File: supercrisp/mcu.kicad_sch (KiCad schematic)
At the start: 9 parts, among them P1 USB_C_Plug_USB2.0, U1 STM32F072CBTx, U2 USBLC6-2SC6

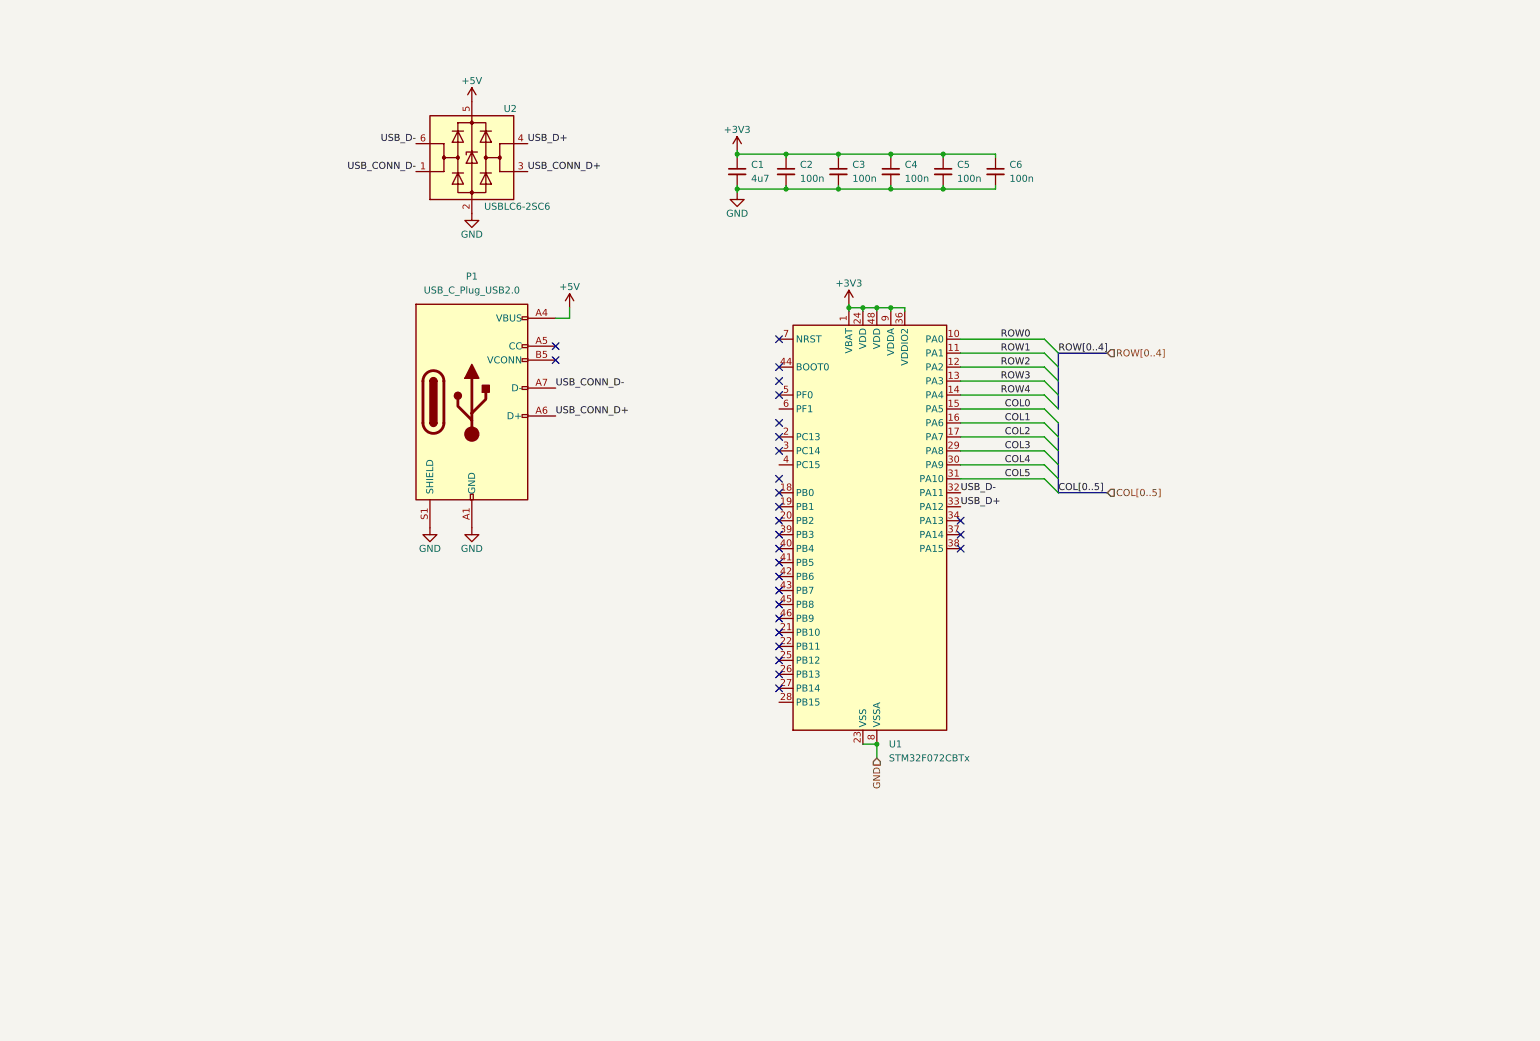
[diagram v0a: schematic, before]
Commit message: Add BOOT0 handling and start working on power schematics
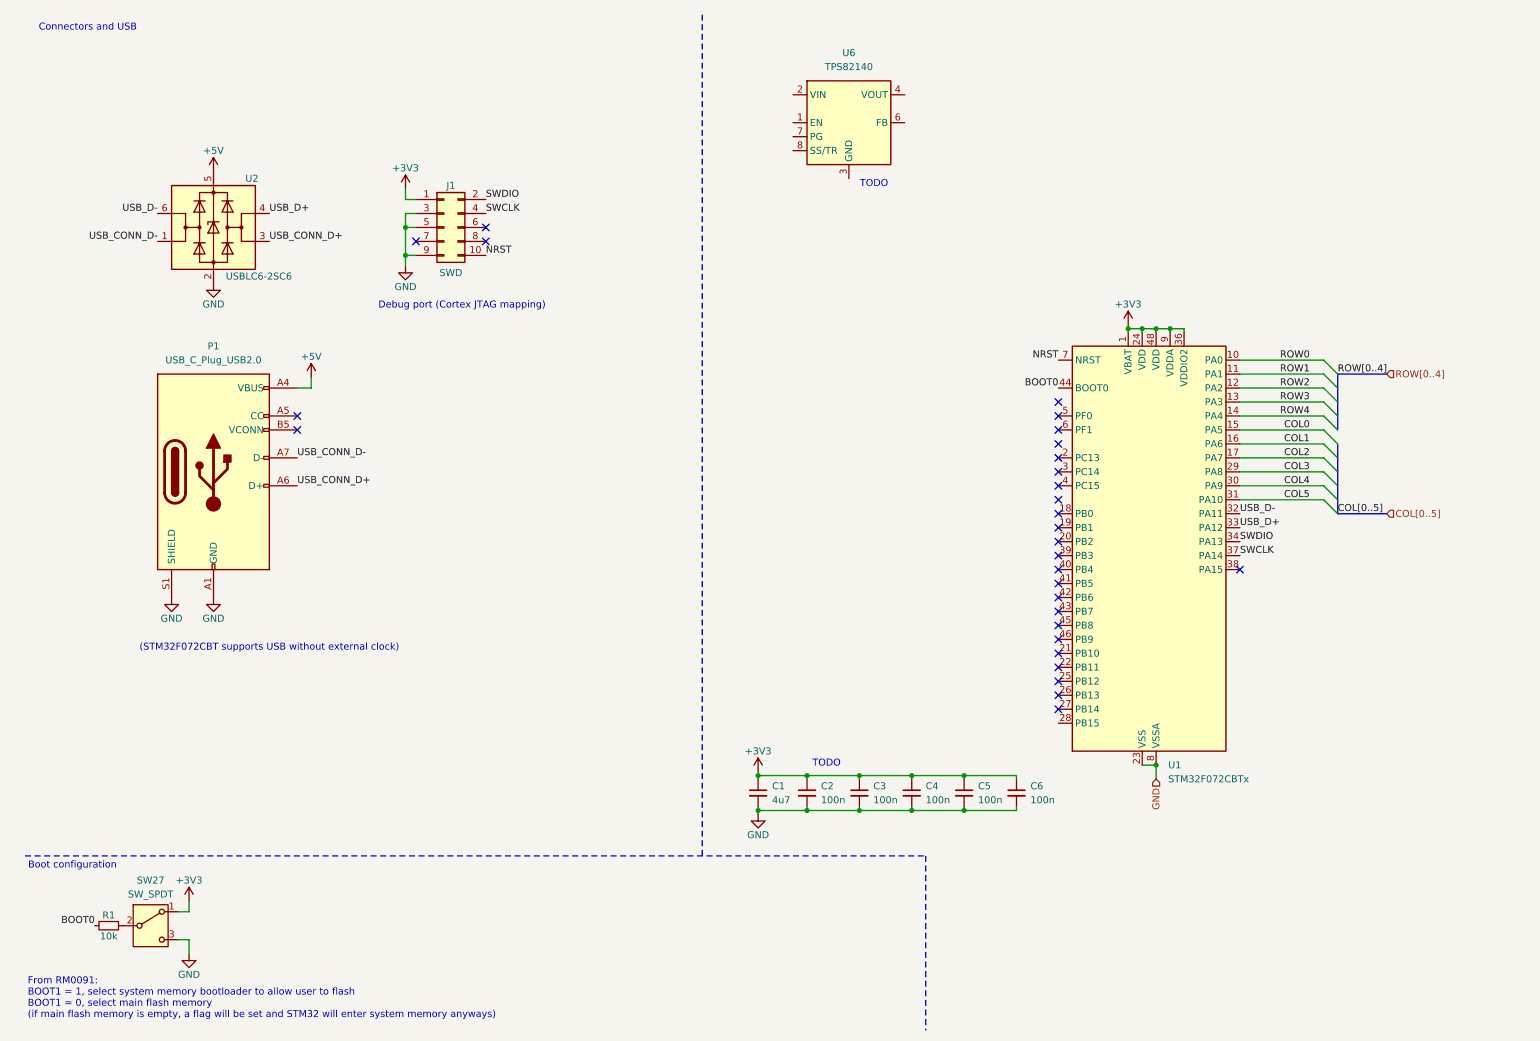
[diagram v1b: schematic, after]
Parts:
- added J1: SWD, Connector_PinHeader_1.27mm:PinHeader_2x05_P1.27mm_Vertical_SMD, symbol Connector_Generic:Conn_02x05_Odd_Even
- added R1: 10k, Resistor_SMD:R_0402_1005Metric, symbol Device:R_Small
- added SW27: SW_SPDT, Button_Switch_SMD:SW_SPDT_PCM12, symbol Switch:SW_SPDT
- added U6: TPS82140, Package_LGA:Texas_SIL0008D_MicroSiP-8-1EP_2.8x3mm_P0.65mm_EP1.1x1.9mm_ThermalVias, symbol Regulator_Switching:TPS82140
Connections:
- net +3V3: now also J1.1 (Pin_1), SW27.1 (A)
- net GND: now also J1.3 (Pin_3), J1.5 (Pin_5), J1.9 (Pin_9), SW27.3 (C)
- net SWDIO: now reaches U1.34 (PA13)
- net SWDIO: now also J1.2 (Pin_2)
- net SWCLK: now reaches U1.37 (PA14)
- net SWCLK: now also J1.4 (Pin_4)
- net BOOT0: now reaches U1.44 (BOOT0)
- net BOOT0: now also R1.2
- net NRST: now reaches U1.7 (NRST)
- net NRST: now also J1.10 (Pin_10)
- new net: U6.3 (GND), U6.9 (GND)
- new net: U6.4 (VOUT), U6.5 (VOUT)
- new net: R1.1, SW27.2 (B)
- no-connect marks 28 -> 29
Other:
- note added: "(STM32F072CBT supports USB without external clock)"
- note added: "Boot configuration"
- note added: "Connectors and USB"
- note added: "Debug port (Cortex JTAG mapping)"
- note added: "From RM0091: BOOT1 = 1, select system memory bootloader to allow user to flash BOOT1 = 0, select main flash memory (if main flash memory is empty, a flag will be set and STM32 will enter system memory anyways)"
- note added: "TODO"
- moved on the sheet: P1, U1, U2

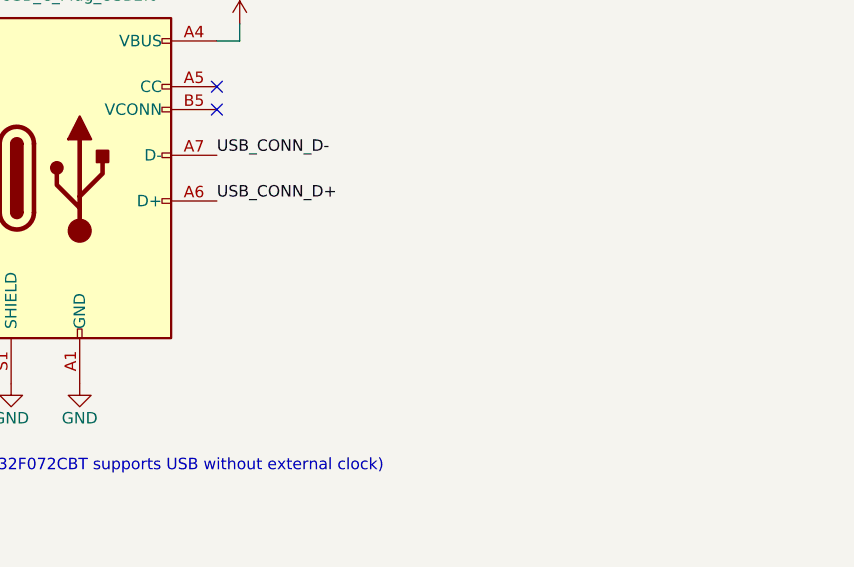
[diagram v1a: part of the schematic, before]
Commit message: Start adding USB C connector circuit
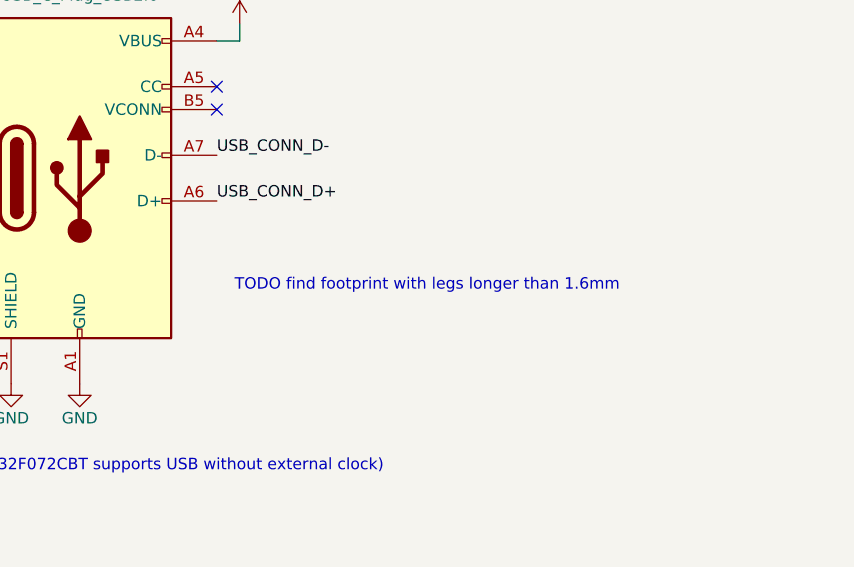
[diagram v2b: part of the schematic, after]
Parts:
- P1: footprint Connector_USB:USB_C_Receptacle_GCT_USB4125-xx-x-0190_6P_TopMnt_Horizontal -> Connector_USB:USB_C_Receptacle_XKB_U262-16XN-4BVC11
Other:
- note added: "TODO find footprint with legs longer than 1.6mm"
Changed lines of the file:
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@@
+		)
+	)
+	(text "TODO find footprint with legs longer than 1.6mm"
+		(exclude_from_sim no)
+		(at 85.598 108.458 0)
+		(effects
+			(font
+				(size 1.27 1.27)
+			)
 		)
 	)
@@
 			)
 		)
-		(property "Footprint" "Connector_USB:USB_C_Receptacle_GCT_USB4125-xx-x-0190_6P_TopMnt_Horizontal"
+		(property "Footprint" "Connector_USB:USB_C_Receptacle_XKB_U262-16XN-4BVC11"
 			(at 50.8 96.52 0)
 			(effects

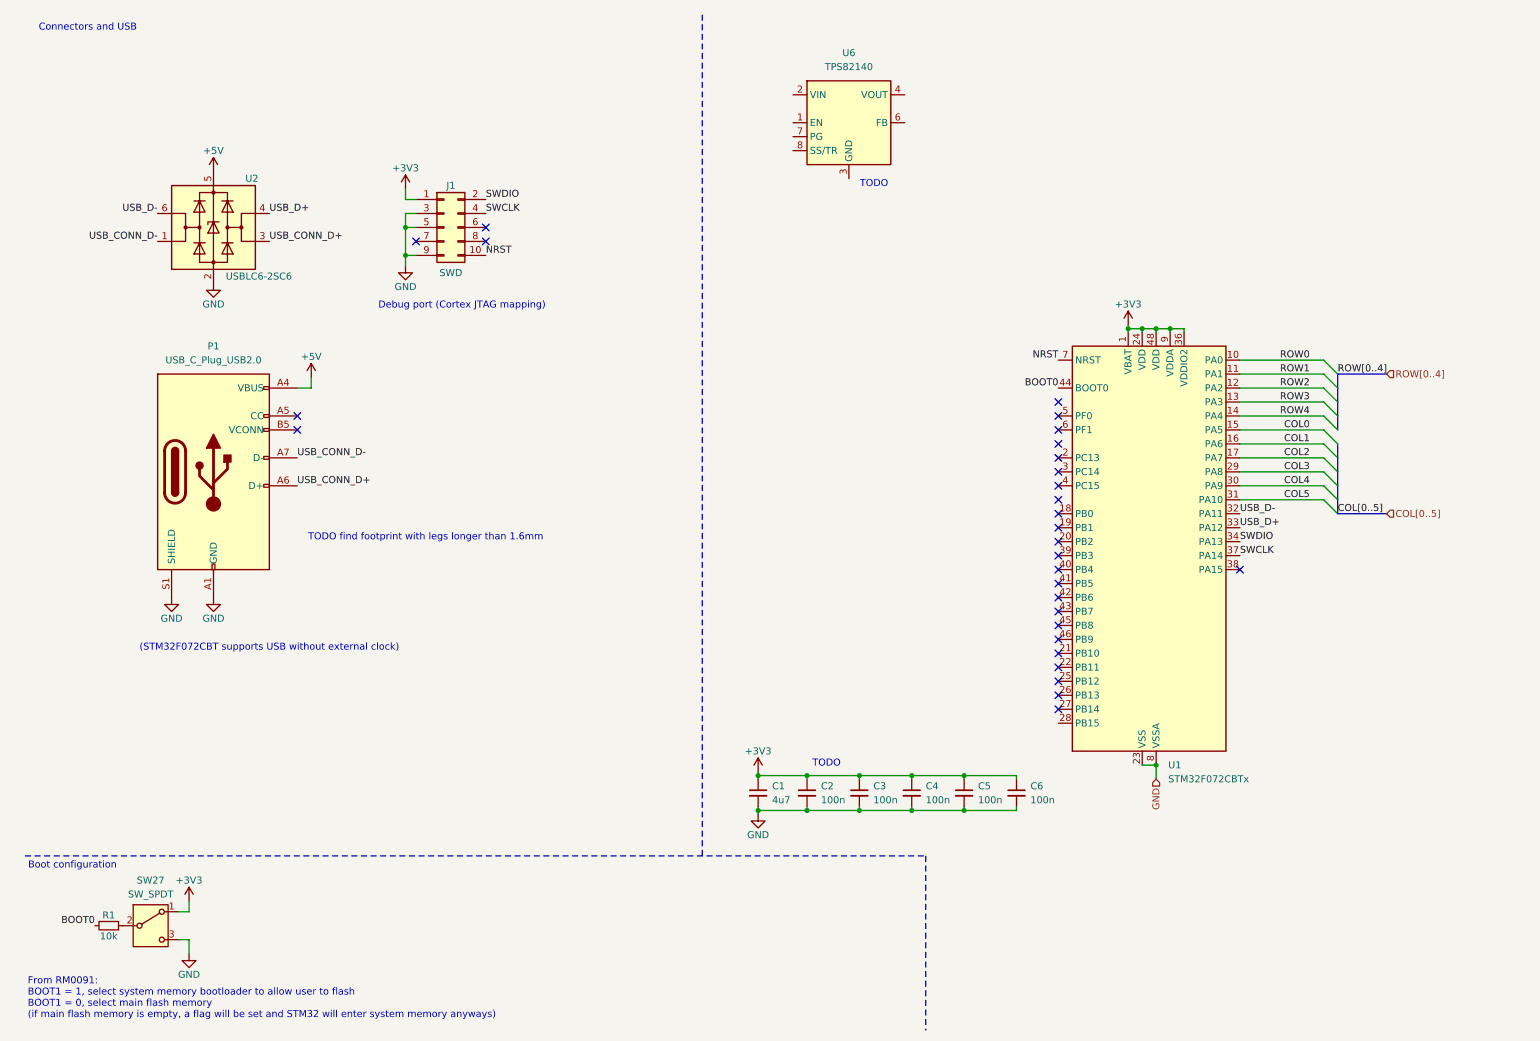
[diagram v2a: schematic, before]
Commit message: Temp placement of switches and usb circuitry
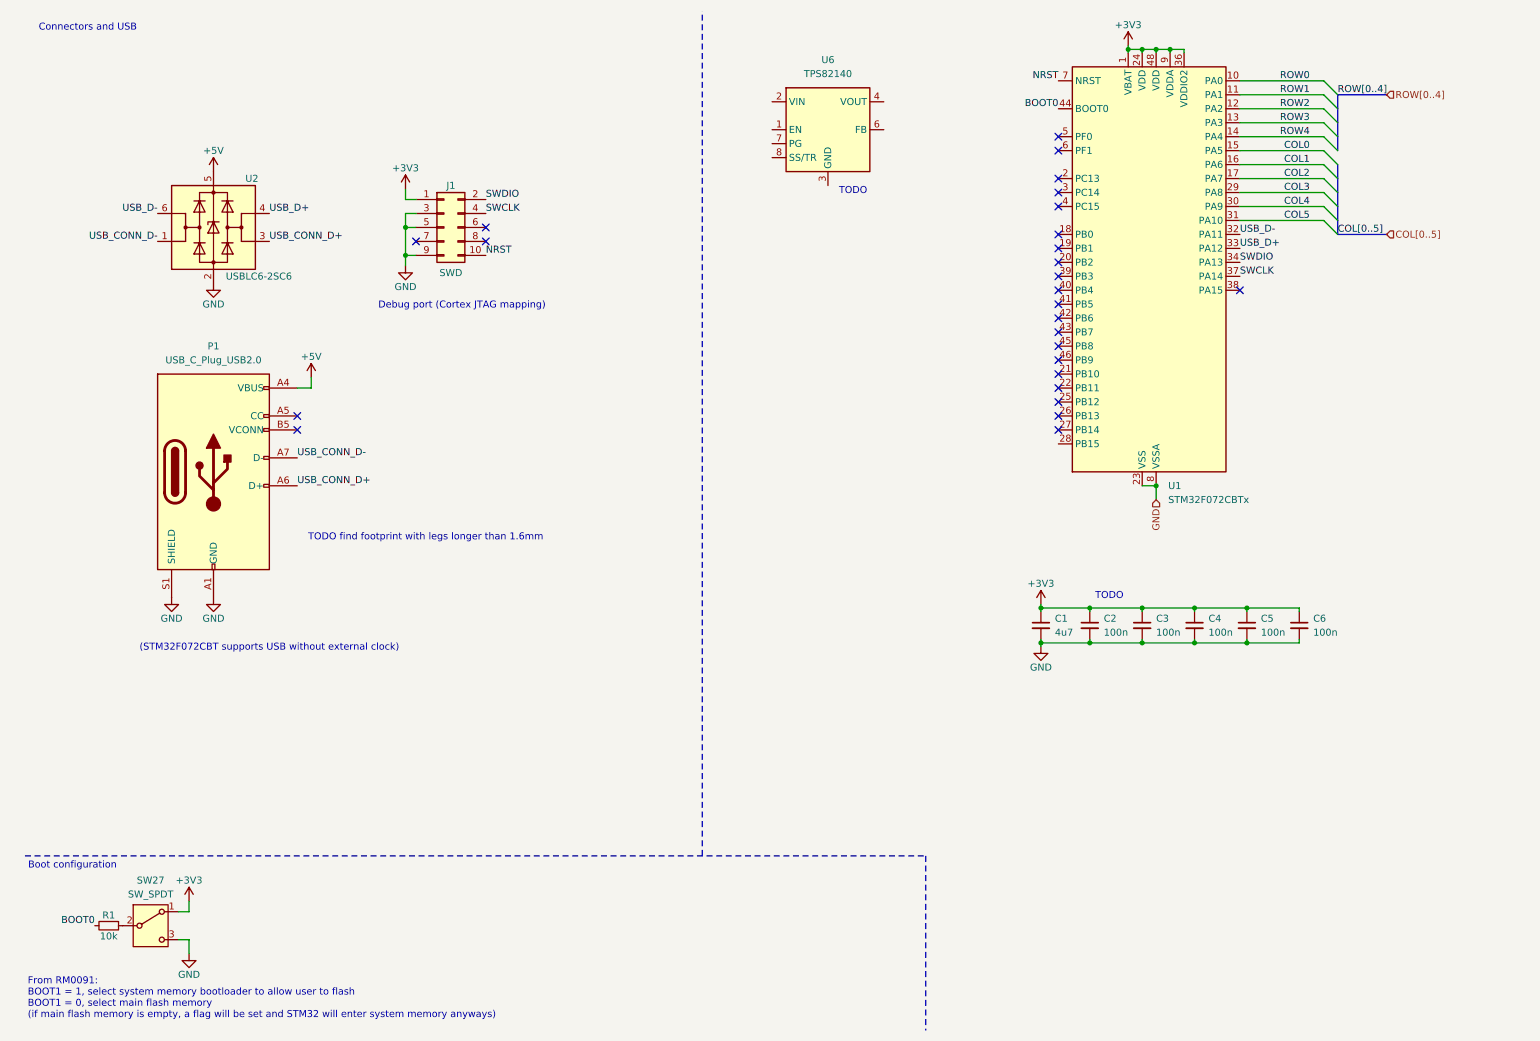
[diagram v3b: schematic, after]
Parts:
- C1: footprint Capacitor_SMD:C_0603_1608Metric -> Capacitor_SMD:C_0603_1608Metric_Pad1.08x0.95mm_HandSolder
- C2, C3, C4, C5, C6: footprint Capacitor_SMD:C_0402_1005Metric -> Capacitor_SMD:C_0603_1608Metric_Pad1.08x0.95mm_HandSolder
- J1: footprint Connector_PinHeader_1.27mm:PinHeader_2x05_P1.27mm_Vertical_SMD -> Connector_PinSocket_1.27mm:PinSocket_2x05_P1.27mm_Vertical_SMD
- R1: footprint Resistor_SMD:R_0402_1005Metric -> Resistor_SMD:R_0603_1608Metric
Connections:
- no-connect marks 29 -> 26
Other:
- moved on the sheet: C1, C2, C3, C4, C5, C6, U1, U6
